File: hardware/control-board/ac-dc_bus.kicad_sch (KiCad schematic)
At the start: 4 parts

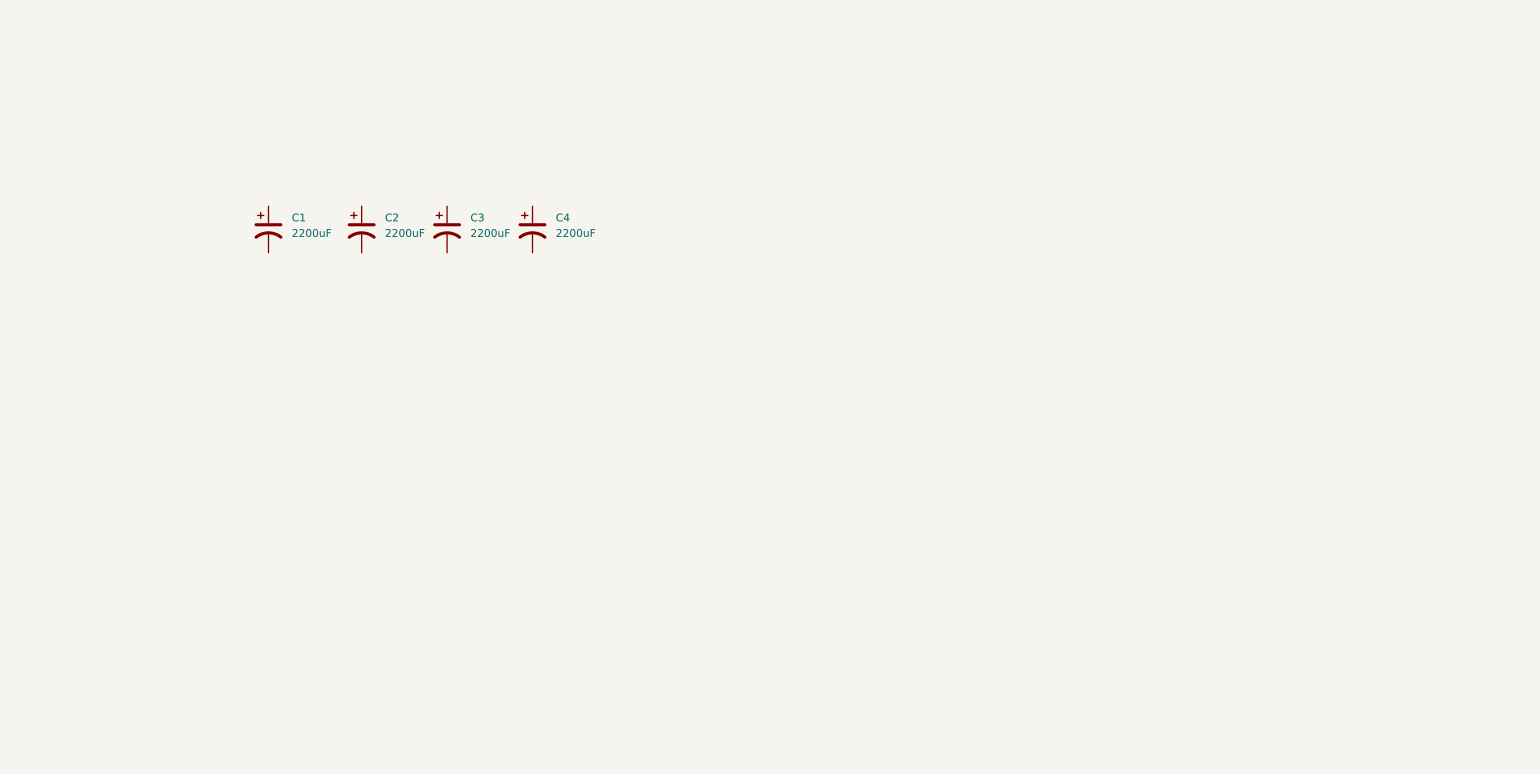
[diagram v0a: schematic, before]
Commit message: added mains ac-dc bus with current sensing
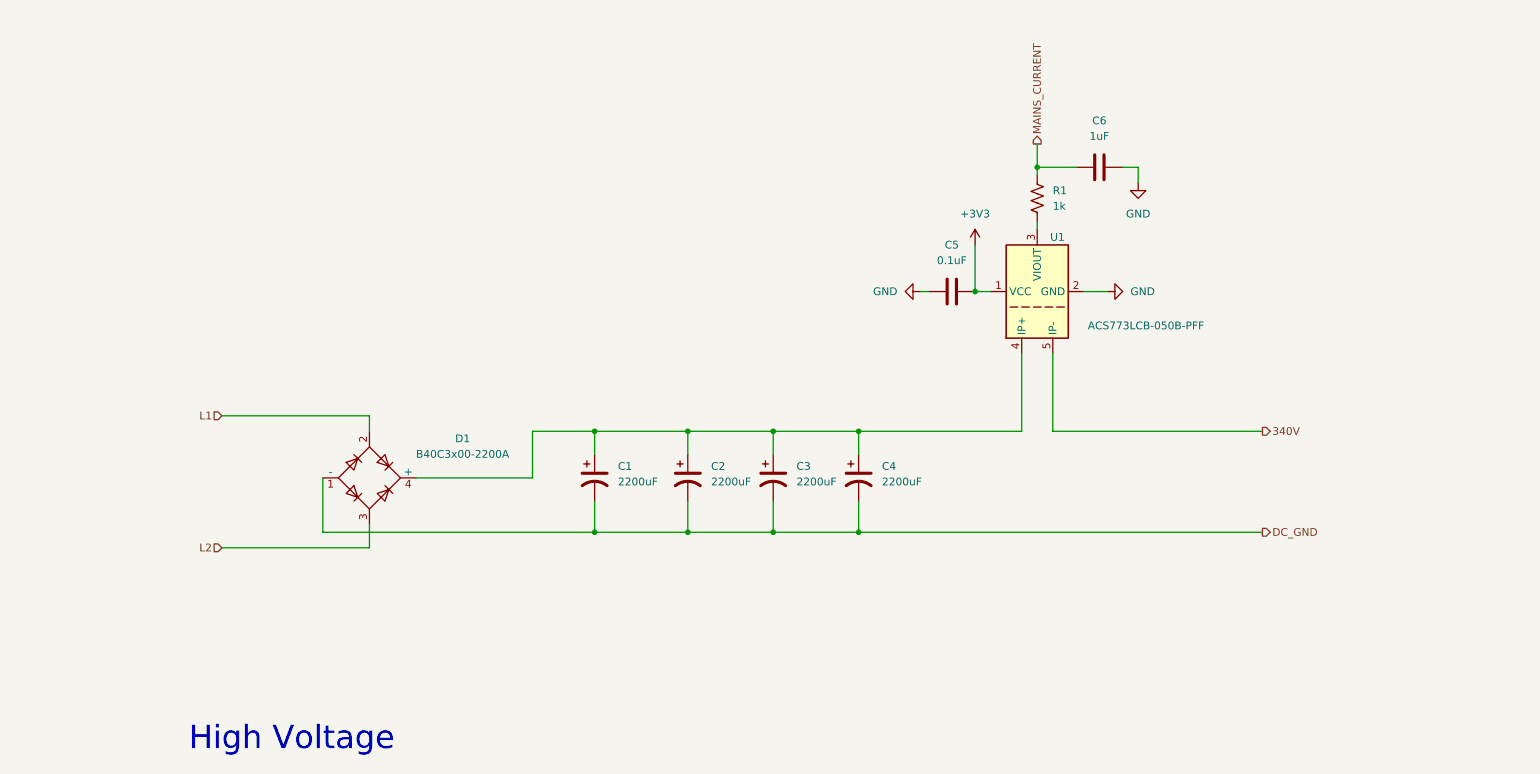
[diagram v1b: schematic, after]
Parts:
- added C5: 0.1uF, symbol Device:C
- added C6: 1uF, symbol Device:C
- added D1: B40C3x00-2200A, Diode_THT:Diode_Bridge_32.0x5.6x17.0mm_P10.0mm_P7.5mm, symbol Diode_Bridge:B40C3x00-2200A
- added R1: 1k, symbol Device:R_US
- added U1: ACS773LCB-050B-PFF, Sensor_Current:Allegro_CB_PFF, symbol Sensor_Current:ACS770xCB-050B-PFF
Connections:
- net at C4.1: now also C1.1, C2.1, C3.1, D1.4 (+), U1.4 (IP+)
- net DC_GND: now reaches C4.2
- net DC_GND: now also C1.2, C2.2, C3.2, D1.1 (-)
- new net: R1.2, U1.3 (VIOUT)
- new net +3V3: C5.2, U1.1 (VCC)
- new net 340V: U1.5 (IP-)
- new net GND: C5.1, C6.2, U1.2 (GND)
- new net L1: D1.2
- new net L2: D1.3
- new net MAINS_CURRENT: C6.1, R1.1
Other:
- note added: "High Voltage"
- moved on the sheet: C1, C2, C3, C4

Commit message: added soft start and bleeder resistor to dc bus
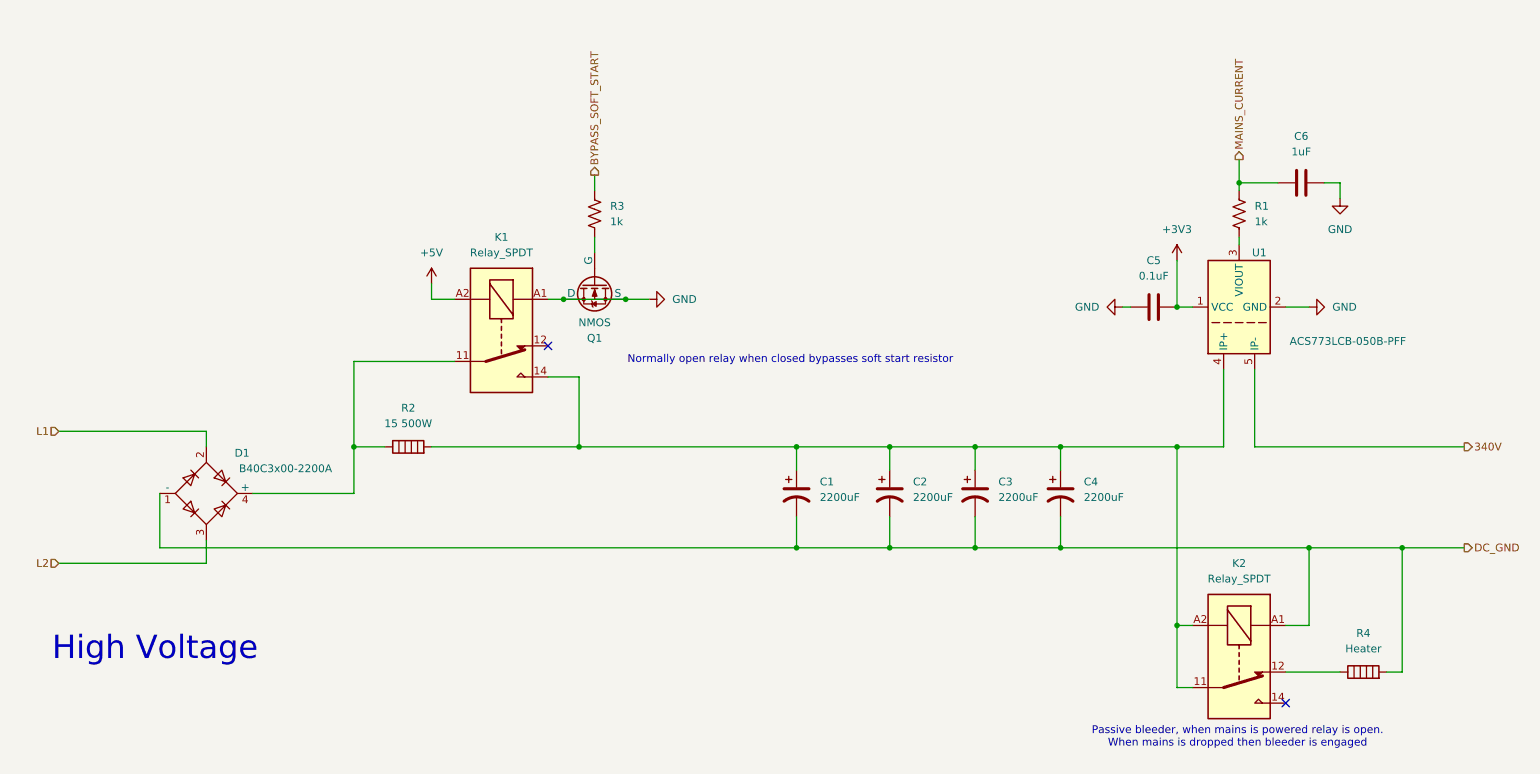
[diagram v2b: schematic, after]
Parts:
- added K1, K2: Relay_SPDT, symbol Relay:Relay_SPDT
- added Q1: NMOS, symbol Simulation_SPICE:NMOS
- added R2: 15 500W, symbol Device:Heater
- added R3: 1k, symbol Device:R_US
- added R4: Heater, symbol Device:Heater
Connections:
- net DC_GND: now also K2.A1, R4.2
- net GND: now also K1.A1, Q1.1 (D), Q1.3 (S)
- net at C1.1, C2.1, C3.1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: now also K1.14, K2.11, K2.A2, R2.2; no longer D1.4 (+)
- new net: D1.4 (+), K1.11, R2.1
- new net: K2.12, R4.1
- new net: Q1.2 (G), R3.2
- new net +5V: K1.A2
- new net BYPASS_SOFT_START: R3.1
- no-connect marks 0 -> 2
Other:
- note added: "Normally open relay when closed bypasses soft start resistor"
- note added: "Passive bleeder, when mains is powered relay is open. When mains is dropped then bleeder is engaged"
- moved on the sheet: C1, C2, C3, C4, C5, C6, D1, R1, U1

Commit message: added voltage divider and start work on inverter and tank circuits
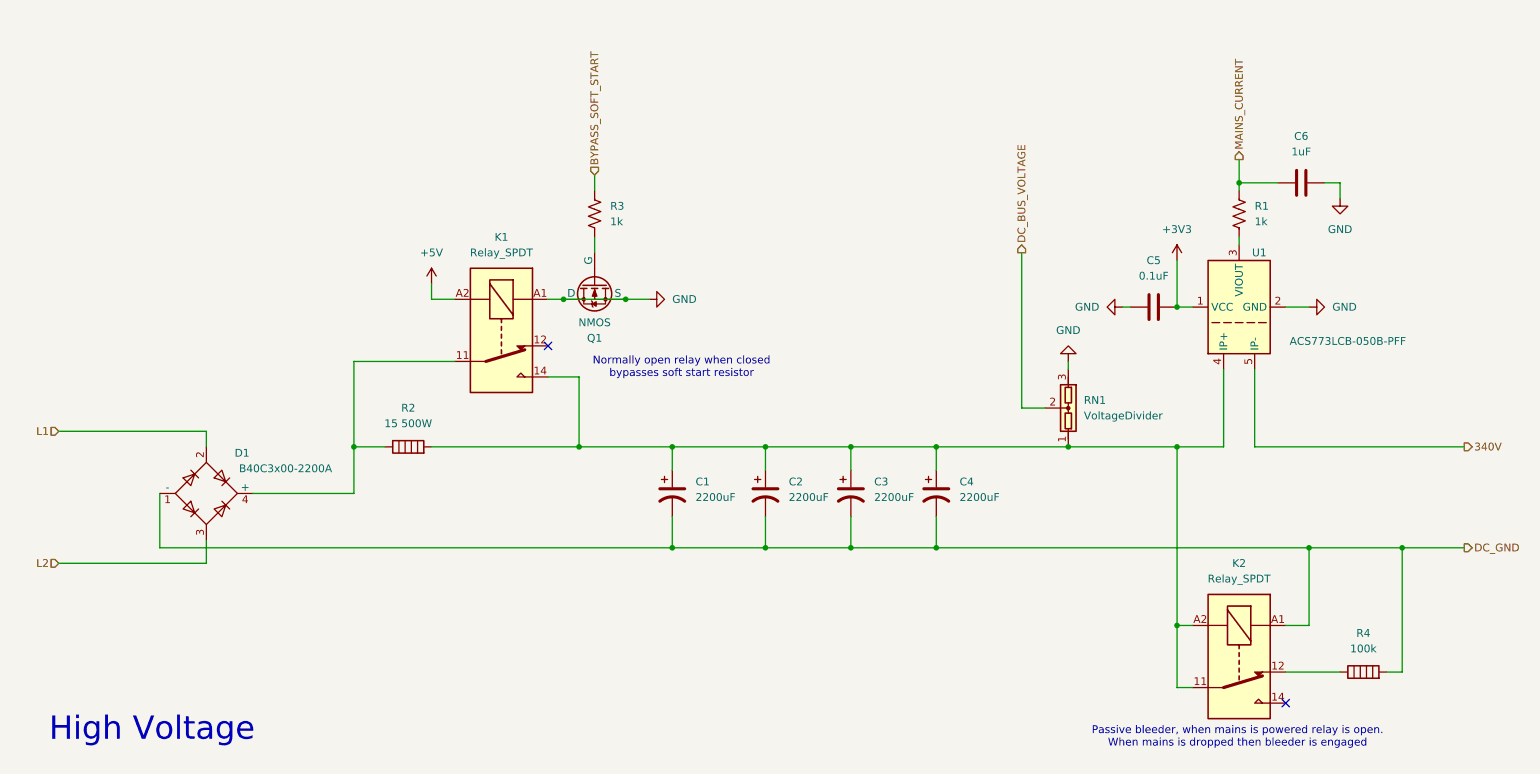
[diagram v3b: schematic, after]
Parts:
- added RN1: VoltageDivider, symbol Device:VoltageDivider
- R4: value Heater -> 100k
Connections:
- net GND: now also RN1.3
- net at C1.1, C2.1, C3.1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: now also RN1.1
- new net DC_BUS_VOLTAGE: RN1.2
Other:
- moved on the sheet: C1, C2, C3, C4

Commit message: progress on mains dc bus design, updated voltage divider with opamp
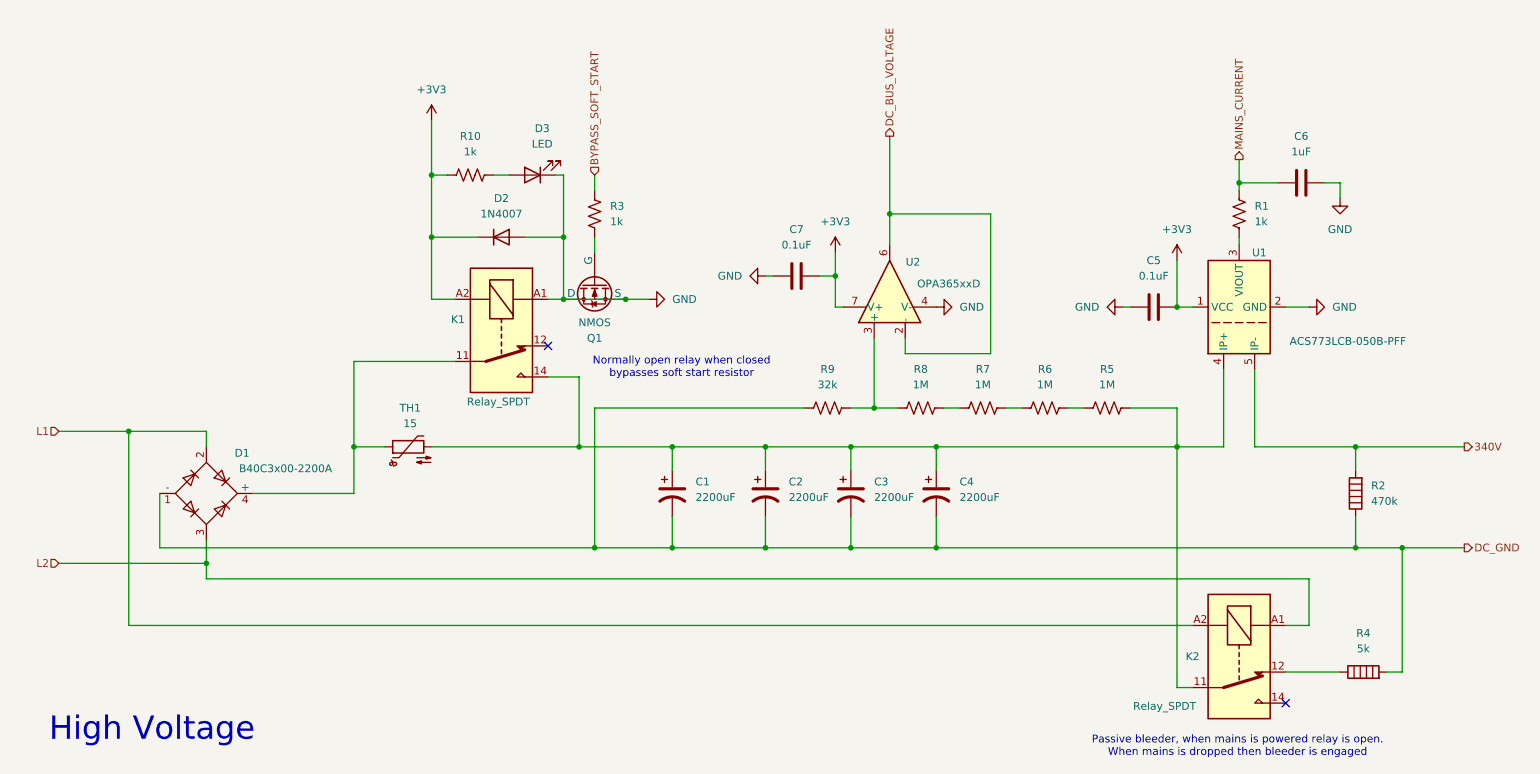
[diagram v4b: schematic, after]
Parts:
- removed RN1: VoltageDivider, symbol Device:VoltageDivider
- added C7: 0.1uF, symbol Device:C
- added D2: 1N4007, Diode_THT:D_DO-41_SOD81_P10.16mm_Horizontal, symbol Diode:1N4007
- added D3: LED, symbol Device:LED
- added R10: 1k, symbol Device:R_US
- added R5, R6, R7, R8: 1M, symbol Device:R_US
- added R9: 32k, symbol Device:R_US
- added TH1: 15, symbol Device:Thermistor_NTC
- added U2: OPA365xxD, Package_SO:SOIC-8_3.9x4.9mm_P1.27mm, symbol Amplifier_Operational:OPA365xxD
- R2: value 15 500W -> 470k
- R4: value 100k -> 5k
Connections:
- net +5V is gone; now on net +3V3: K1.A2
- net +3V3: now also C7.2, D2.1 (K), R10.1, U2.7 (V+)
- net 340V: now also R2.2
- net DC_BUS_VOLTAGE: now also U2.2 (-), U2.6
- net DC_GND: now also R2.1, R9.1; no longer K2.A1
- net GND: now also C7.1, D2.2 (A), D3.1 (K), U2.4 (V-)
- net L1: now also K2.A2
- net L2: now also K2.A1
- net at D1.4 (+), K1.11: now also TH1.1; no longer R2.1
- net at C1.1, C2.1, C3.1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: now also R5.2, TH1.2; no longer K2.A2, R2.2
- new net: R8.1, R9.2, U2.3 (+)
- new net: R7.1, R8.2
- new net: R5.1, R6.2
- new net: D3.2 (A), R10.2
- new net: R6.1, R7.2
